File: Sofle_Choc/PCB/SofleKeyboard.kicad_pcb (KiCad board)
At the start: 2 copper layers, 179.3 x 122 mm, 94 parts, among them J2 4PIN, J3 OLED, P1 i2c_pin, P2 i2c_pin, SW1 SW_PUSH_LED, SW10 SW_PUSH_LED, SW11 SW_PUSH_LED, SW12 SW_PUSH_LED, SW13 SW_PUSH_LED, SW14 SW_PUSH_LED, SW15 SW_PUSH_LED, SW16 SW_PUSH_LED, SW17 SW_PUSH_LED, SW18 SW_PUSH_LED, SW19 SW_PUSH_LED, SW2 SW_PUSH_LED, SW20 SW_PUSH_LED, SW21 SW_PUSH_LED, SW22 SW_PUSH_LED, SW23 SW_PUSH_LED, SW24 SW_PUSH_LED, SW25 Rotary_Encoder_Switch, SW26 SW_PUSH_LED, SW27 SW_PUSH_LED, SW28 SW_PUSH_LED, SW29 SW_PUSH_LED, SW3 SW_PUSH_LED, SW30 SW_PUSH_LED, SW31 SW_PUSH_LED, SW32 SW_PUSH_LED, SW33 SW_PUSH_LED, SW34 SW_PUSH_LED, SW35 SW_PUSH_LED, SW4 SW_PUSH_LED, SW5 SW_PUSH_LED, SW6 SW_PUSH_LED, SW7 SW_PUSH_LED, SW8 SW_PUSH_LED, SW9 SW_PUSH_LED, U1 ProMicro

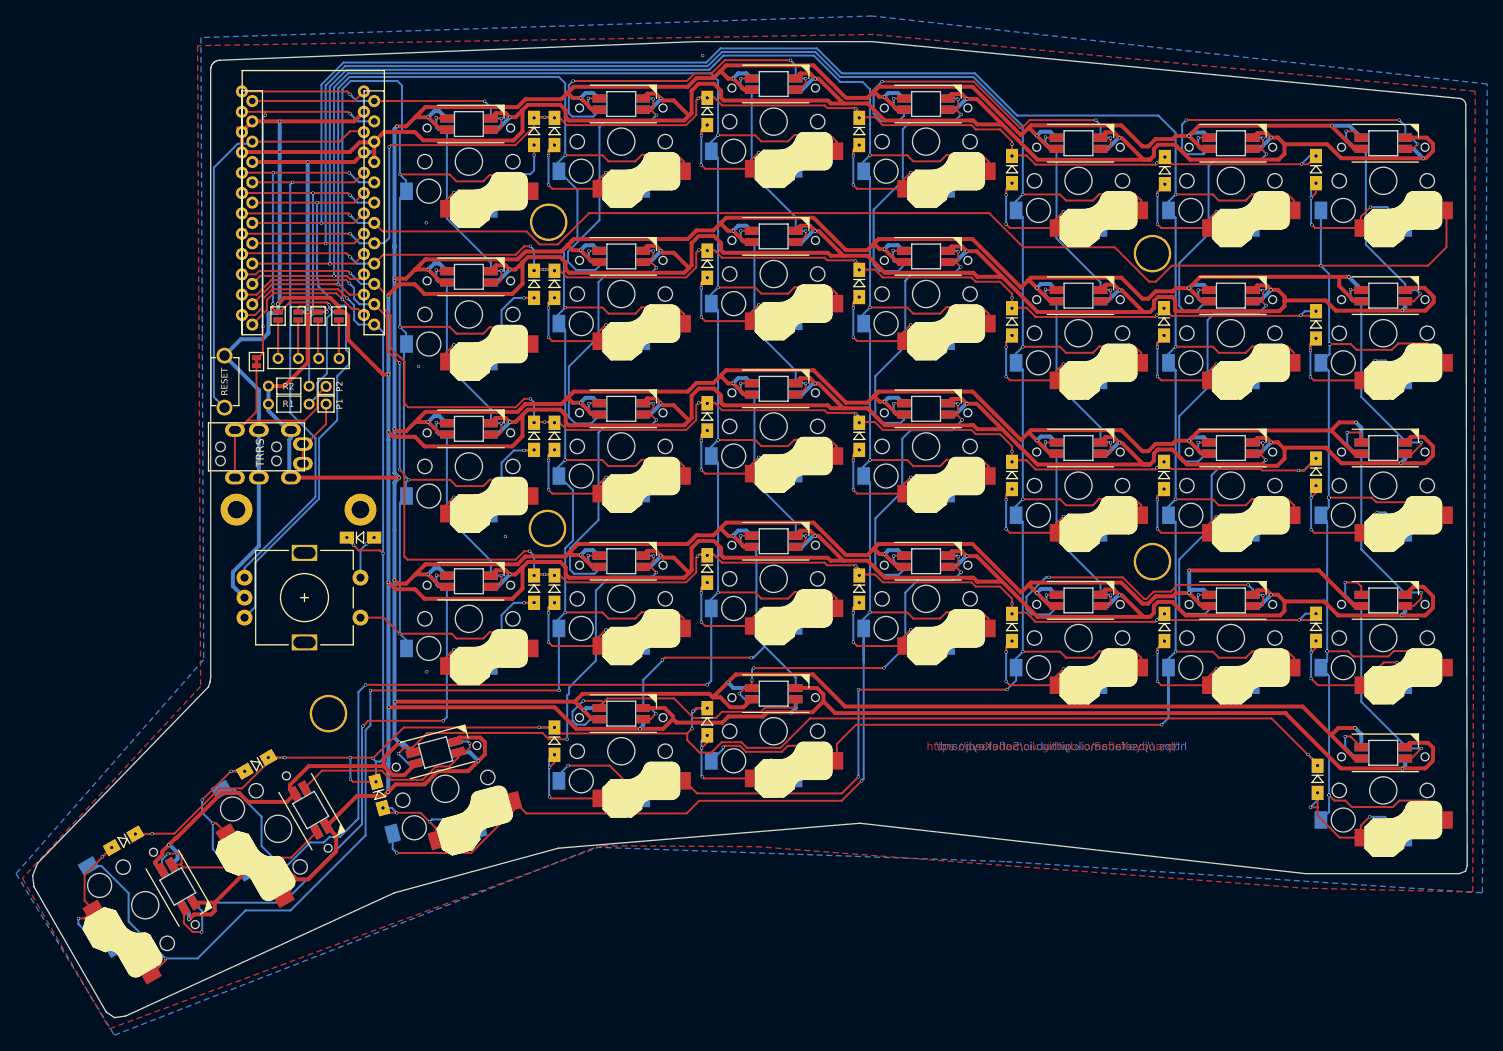
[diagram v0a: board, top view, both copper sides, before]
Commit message: Make more space around diodes
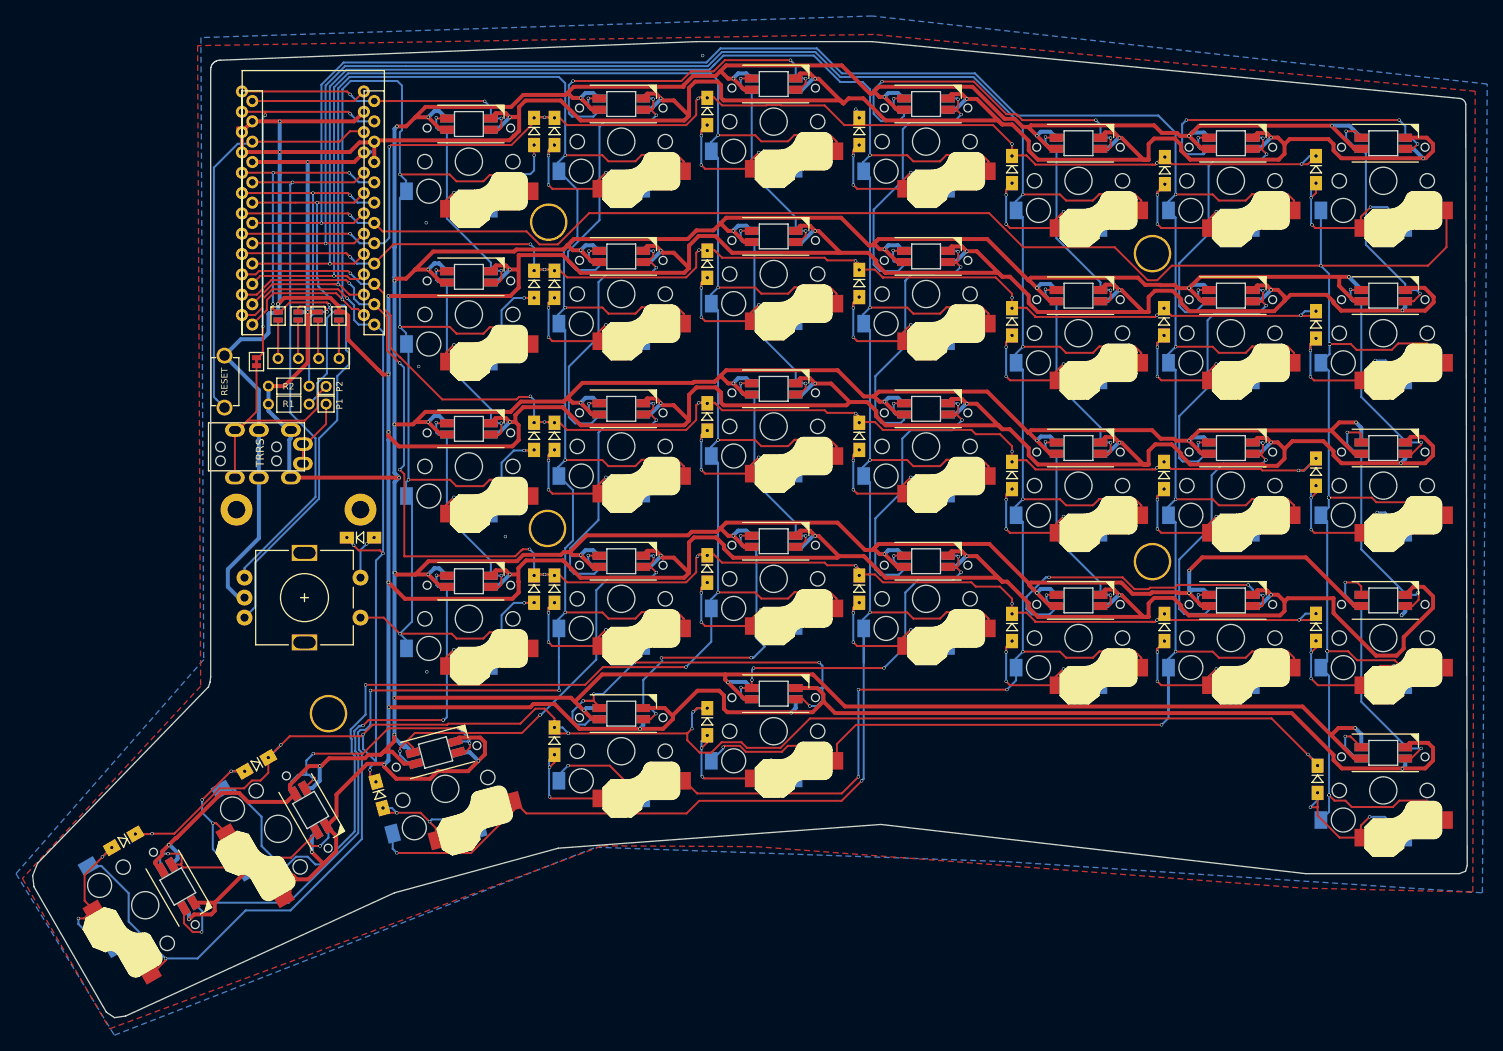
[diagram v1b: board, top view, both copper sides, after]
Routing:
- net GND: track 1273.6 -> 1297.3 mm, vias 47 -> 48
- net Net-(SW29B-DOUT): track 37.1 -> 53.5 mm, vias 1 -> 5
- net Net-(SW27B-DOUT): track 26.5 -> 36.2 mm, vias 1 -> 4
- net Net-(SW21B-DOUT): track 48.0 -> 41.2 mm
- net VCC: track 1080.8 -> 1074.9 mm, vias 41 -> 42
- net Net-(SW26B-DOUT): track 25.5 -> 30.8 mm, vias 1 -> 2
- net row2: track 170.8 -> 167.3 mm
- net row4: track 268.7 -> 271.9 mm, vias 12 -> 11
- net Net-(SW20B-DIN): track 60.1 -> 57.1 mm
- net col6: track 308.4 -> 310.7 mm
- net row0: track 167.7 -> 166.4 mm
- net Net-(SW19B-DOUT): track 77.3 -> 78.4 mm
- net Net-(SW23B-DOUT): track 45.4 -> 44.4 mm
- net col3: track 326.3 -> 325.4 mm
- net Net-(SW4B-DOUT): track 49.5 -> 48.6 mm
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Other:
- outline, holes or cut-outs redrawn
- board text removed: "https://josefadamcik.github.io/SofleKeyboard/"

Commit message: Increase via size and fix clearance
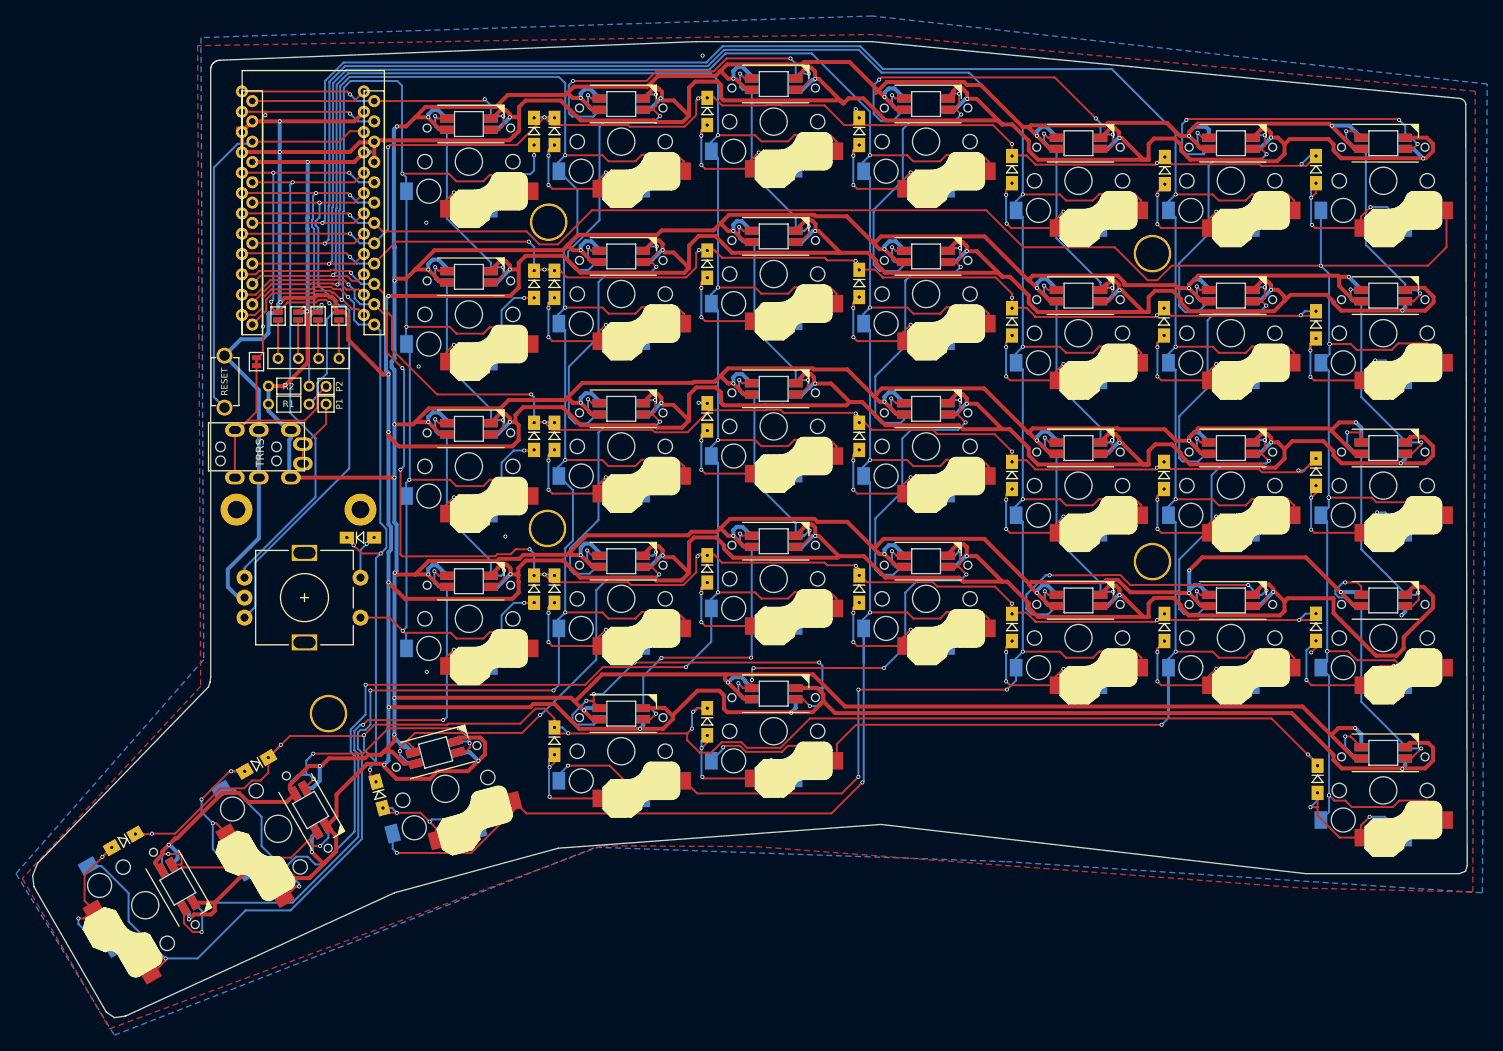
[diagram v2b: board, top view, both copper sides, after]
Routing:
- net VCC: track 1074.9 -> 1104.1 mm, vias 42 -> 43
- net GND: track 1297.3 -> 1321.0 mm
- net Net-(SW22B-DIN): track 47.2 -> 51.0 mm
- net Net-(SW14B-DIN): track 39.8 -> 42.9 mm
- net Net-(SW16B-DIN): track 40.2 -> 43.1 mm
- net Net-(SW2B-DOUT): track 47.0 -> 49.8 mm
- net Net-(SW2B-DIN): track 40.8 -> 43.5 mm
- net Net-(SW23B-DOUT): track 44.4 -> 46.9 mm
- net Net-(SW15B-DOUT): track 27.4 -> 29.9 mm
- net Net-(SW15B-DIN): track 27.4 -> 29.8 mm
- net Net-(SW3B-DOUT): track 27.4 -> 29.7 mm
- net SW25A: track 201.3 -> 199.0 mm
- net Net-(SW14B-DOUT): track 40.3 -> 42.6 mm
- net Net-(SW4B-DOUT): track 48.6 -> 50.8 mm
- net Net-(SW10B-DIN): track 40.4 -> 42.6 mm
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
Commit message: Move mounting holes
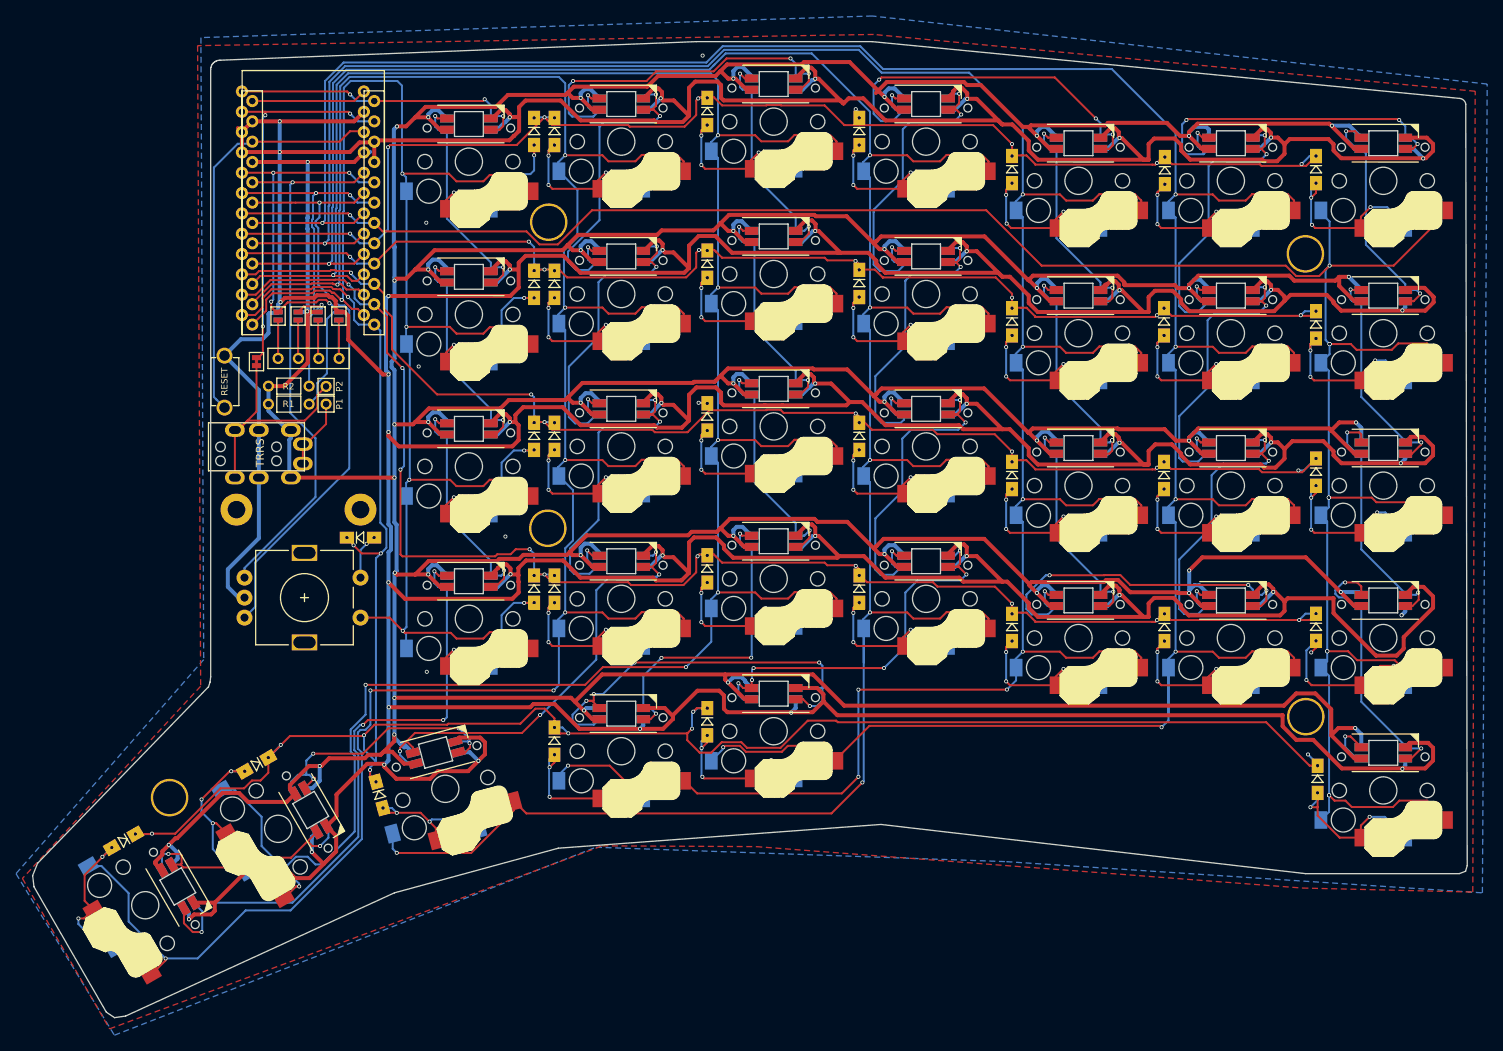
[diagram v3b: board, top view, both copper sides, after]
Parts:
- moved TH6 27.3 mm to (225.3, 119.4)
- moved TH7 22.5 mm to (83.1, 129.5)
- moved TH4 19.1 mm to (225.3, 61.8)
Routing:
- net VCC: track 1104.1 -> 1107.7 mm
- net col6: track 311.0 -> 308.5 mm
- net col0: track 357.5 -> 356.7 mm
